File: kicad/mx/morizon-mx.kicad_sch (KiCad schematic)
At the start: 145 parts, among them SW1 SW_Push, SW10 SW_Push, SW11 SW_Push, SW12 SW_Push, SW13 SW_Push, SW14 SW_Push, SW15 SW_Push, SW16 SW_Push, SW17 SW_Push, SW18 SW_Push, SW19 SW_Push, SW2 SW_Push, SW20 SW_Push, SW21 SW_Push, SW22 SW_Push, SW23 SW_Push, SW24 SW_Push, SW25 SW_Push, SW26 SW_Push, SW27 SW_Push, SW28 SW_Push, SW29 SW_Push, SW3 SW_Push, SW30 SW_Push, SW31 SW_Push, SW32 SW_Push, SW33 SW_Push, SW34 SW_Push, SW35 SW_Push, SW36 SW_Push, SW37 SW_Push, SW38 SW_Push, SW39 SW_Push, SW4 SW_Push, SW40 SW_Push, SW41 SW_Push, SW42 SW_Push, SW43 SW_Push, SW44 SW_Push, SW45 SW_Push, SW46 SW_Push, SW47 SW_Push, SW48 SW_Push, SW49 SW_Push, SW5 SW_Push, SW50 SW_Push, SW51 SW_Push, SW52 SW_Push, SW53 SW_Push, SW54 SW_Push, SW55 SW_Push, SW56 SW_Push, SW57 SW_Push, SW58 SW_Push, SW59 SW_Push, SW6 SW_Push, SW60 SW_Push, SW61 SW_Push, SW62 SW_Push, SW63 SW_Push, SW64 SW_Push, SW65 SW_Push, SW66 SW_Push, SW7 SW_Push, SW8 SW_Push, SW9 SW_Push, U1 PRO-MICRO

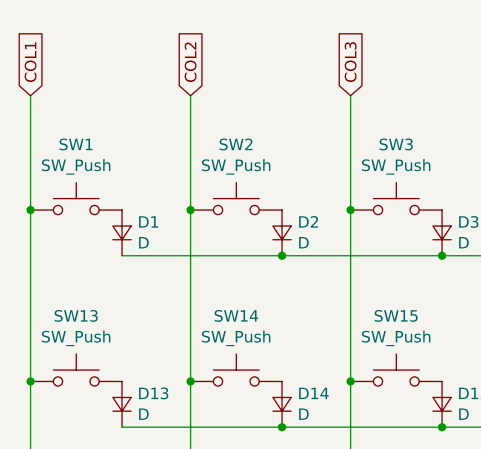
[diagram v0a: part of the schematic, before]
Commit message: Use KiCad 6 symbol library format
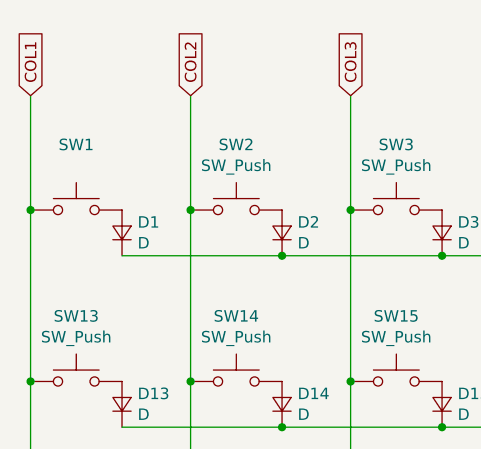
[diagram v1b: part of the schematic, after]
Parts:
- SW1: value SW_Push -> (none); footprint horizon-footprints:SW_MX -> (none)
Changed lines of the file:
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@@
     (in_bom yes) (on_board yes)
     (property "Reference" "SW1" (id 0) (at 22.86 27.051 0))
-    (property "Value" "SW_Push" (id 1) (at 22.86 29.3624 0))
-    (property "Footprint" "horizon-footprints:SW_MX" (id 2) (at 22.86 29.21 0)
+    (property "Value" "" (id 1) (at 22.86 29.3624 0))
+    (property "Footprint" "" (id 2) (at 22.86 29.21 0)
       (effects (font (size 1.27 1.27)) hide)
     )

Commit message: Upgrade project files to KiCad 7
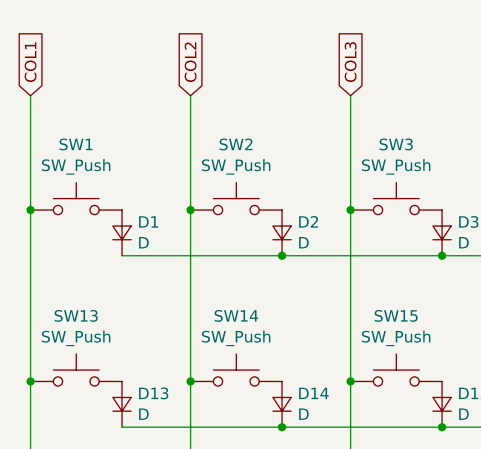
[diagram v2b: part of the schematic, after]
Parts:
- SW1: value (none) -> SW_Push; footprint (none) -> horizon-footprints:SW_MX
